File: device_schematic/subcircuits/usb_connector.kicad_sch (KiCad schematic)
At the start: 3 parts, among them J1 USB_B

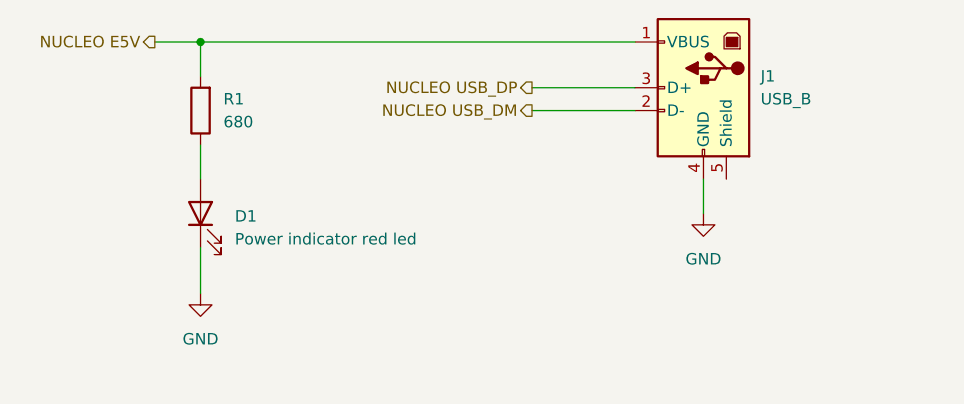
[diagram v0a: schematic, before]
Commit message: Device schematic finished version
+ correction to use D7 in place of D13
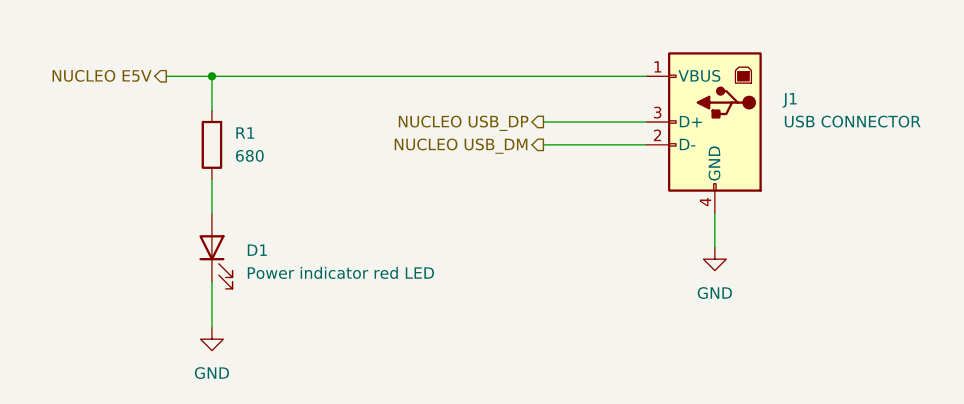
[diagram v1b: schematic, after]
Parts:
- D1: value Power indicator red led -> Power indicator red LED
- J1: value USB_B -> USB CONNECTOR
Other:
- moved on the sheet: D1, R1
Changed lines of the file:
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@@
 (kicad_sch (version 20211123) (generator eeschema)
   (paper "A4")
-  (junction (at 125.73 74.93) (diameter 0) (color 0 0 0 0)
+  (junction (at 127 78.74) (diameter 0) (color 0 0 0 0)
   )
-  (wire (pts (xy 162.56 82.55) (xy 173.99 82.55))
+  (wire (pts (xy 163.83 86.36) (xy 175.26 86.36))
     (stroke (width 0) (type default) (color 0 0 0 0))
   )
-  (wire (pts (xy 125.73 97.79) (xy 125.73 102.87))
+  (wire (pts (xy 127 101.6) (xy 127 106.68))
     (stroke (width 0) (type default) (color 0 0 0 0))
   )
-  (wire (pts (xy 125.73 74.93) (xy 125.73 78.74))
+  (wire (pts (xy 127 78.74) (xy 127 82.55))
     (stroke (width 0) (type default) (color 0 0 0 0))
   )
-  (wire (pts (xy 125.73 86.36) (xy 125.73 90.17))
+  (wire (pts (xy 127 90.17) (xy 127 93.98))
     (stroke (width 0) (type default) (color 0 0 0 0))
   )
-  (wire (pts (xy 181.61 90.17) (xy 181.61 93.98))
+  (wire (pts (xy 182.88 93.98) (xy 182.88 97.79))
     (stroke (width 0) (type default) (color 0 0 0 0))
   )
-  (wire (pts (xy 162.56 80.01) (xy 173.99 80.01))
+  (wire (pts (xy 163.83 83.82) (xy 175.26 83.82))
     (stroke (width 0) (type default) (color 0 0 0 0))
   )
-  (wire (pts (xy 125.73 74.93) (xy 173.99 74.93))
+  (wire (pts (xy 127 78.74) (xy 175.26 78.74))
     (stroke (width 0) (type default) (color 0 0 0 0))
   )
-  (wire (pts (xy 120.65 74.93) (xy 125.73 74.93))
+  (wire (pts (xy 121.92 78.74) (xy 127 78.74))
     (stroke (width 0) (type default) (color 0 0 0 0))
   )
-  (hierarchical_label "NUCLEO USB_DM" (shape output) (at 162.56 82.55 180)
+  (hierarchical_label "NUCLEO USB_DM" (shape output) (at 163.83 86.36 180)
     (effects (font (size 1.27 1.27)) (justify right))
   )
-  (hierarchical_label "NUCLEO USB_DP" (shape output) (at 162.56 80.01 180)
+  (hierarchical_label "NUCLEO USB_DP" (shape output) (at 163.83 83.82 180)
     (effects (font (size 1.27 1.27)) (justify right))
   )
-  (hierarchical_label "NUCLEO E5V" (shape output) (at 120.65 74.93 180)
+  (hierarchical_label "NUCLEO E5V" (shape output) (at 121.92 78.74 180)
     (effects (font (size 1.27 1.27)) (justify right))
   )
-  (symbol (lib_id "Device:R") (at 125.73 82.55 180) (unit 1)
+  (symbol (lib_id "Device:R") (at 127 86.36 180) (unit 1)
     (in_bom yes) (on_board yes) (fields_autoplaced)
-    (property "Reference" "R1" (id 0) (at 128.27 81.2799 0)
+    (property "Reference" "R1" (id 0) (at 129.54 85.0899 0)
       (effects (font (size 1.27 1.27)) (justify right))
     )
-    (property "Value" "680" (id 1) (at 128.27 83.8199 0)
+    (property "Value" "680" (id 1) (at 129.54 87.6299 0)
       (effects (font (size 1.27 1.27)) (justify right))
     )
-    (property "Footprint" "" (id 2) (at 127.508 82.55 90)
+    (property "Footprint" "" (id 2) (at 128.778 86.36 90)
       (effects (font (size 1.27 1.27)) hide)
     )
-    (property "Datasheet" "~" (id 3) (at 125.73 82.55 0)
+    (property "Datasheet" "~" (id 3) (at 127 86.36 0)
       (effects (font (size 1.27 1.27)) hide)
     )
@@
     (pin "2")
   )
-  (symbol (lib_id "Device:LED") (at 125.73 93.98 90) (unit 1)
+  (symbol (lib_id "Device:LED") (at 127 97.79 90) (unit 1)
     (in_bom yes) (on_board yes) (fields_autoplaced)
-    (property "Reference" "D1" (id 0) (at 129.54 94.2974 90)
+    (property "Reference" "D1" (id 0) (at 130.81 98.1074 90)
       (effects (font (size 1.27 1.27)) (justify right))
     )
-    (property "Value" "Power indicator red led" (id 1) (at 129.54 96.8374 90)
+    (property "Value" "Power indicator red LED" (id 1) (at 130.81 100.6474 90)
       (effects (font (size 1.27 1.27)) (justify right))
     )
-    (property "Footprint" "" (id 2) (at 125.73 93.98 0)
+    (property "Footprint" "" (id 2) (at 127 97.79 0)
       (effects (font (size 1.27 1.27)) hide)
     )
-    (property "Datasheet" "~" (id 3) (at 125.73 93.98 0)
+    (property "Datasheet" "~" (id 3) (at 127 97.79 0)
       (effects (font (size 1.27 1.27)) hide)
     )
@@
     (pin "2")
   )
-  (symbol (lib_id "Connector:USB_B") (at 181.61 80.01 0) (mirror y) (unit 1)
-    (in_bom yes) (on_board yes) (fields_autoplaced)
-    (property "Reference" "J1" (id 0) (at 187.96 78.7399 0)
+  (symbol (lib_id "Connector:USB_B") (at 182.88 83.82 0) (mirror y) (unit 1)
+    (in_bom yes) (on_board yes)
+    (property "Reference" "J1" (id 0) (at 190.5 81.28 0)
       (effects (font (size 1.27 1.27)) (justify right))
     )
-    (property "Value" "USB_B" (id 1) (at 187.96 81.2799 0)
+    (property "Value" "USB CONNECTOR" (id 1) (at 190.5 83.82 0)
       (effects (font (size 1.27 1.27)) (justify right))
     )
-    (property "Footprint" "" (id 2) (at 177.8 81.28 0)
+    (property "Footprint" "" (id 2) (at 186.69 85.09 0)
       (effects (font (size 1.27 1.27)) hide)
     )
-    (property "Datasheet" " ~" (id 3) (at 177.8 81.28 0)
+    (property "Datasheet" " ~" (id 3) (at 186.69 85.09 0)
       (effects (font (size 1.27 1.27)) hide)
     )
@@
     (pin "3")
     (pin "4")
-    (pin "5")
   )
-  (symbol (lib_id "power:GND") (at 181.61 93.98 0) (unit 1)
+  (symbol (lib_id "power:GND") (at 182.88 97.79 0) (unit 1)
     (in_bom yes) (on_board yes) (fields_autoplaced)
-    (property "Reference" "#PWR?" (id 0) (at 181.61 100.33 0)
+    (property "Reference" "#PWR?" (id 0) (at 182.88 104.14 0)
       (effects (font (size 1.27 1.27)) hide)
     )
-    (property "Value" "GND" (id 1) (at 181.61 99.06 0))
-    (property "Footprint" "" (id 2) (at 181.61 93.98 0)
+    (property "Value" "GND" (id 1) (at 182.88 102.87 0))
+    (property "Footprint" "" (id 2) (at 182.88 97.79 0)
       (effects (font (size 1.27 1.27)) hide)
     )
-    (property "Datasheet" "" (id 3) (at 181.61 93.98 0)
+    (property "Datasheet" "" (id 3) (at 182.88 97.79 0)
       (effects (font (size 1.27 1.27)) hide)
     )
     (pin "1")
   )
-  (symbol (lib_id "power:GND") (at 125.73 102.87 0) (unit 1)
+  (symbol (lib_id "power:GND") (at 127 106.68 0) (unit 1)
     (in_bom yes) (on_board yes) (fields_autoplaced)
-    (property "Reference" "#PWR?" (id 0) (at 125.73 109.22 0)
+    (property "Reference" "#PWR?" (id 0) (at 127 113.03 0)
       (effects (font (size 1.27 1.27)) hide)
     )
-    (property "Value" "GND" (id 1) (at 125.73 107.95 0))
-    (property "Footprint" "" (id 2) (at 125.73 102.87 0)
+    (property "Value" "GND" (id 1) (at 127 111.76 0))
+    (property "Footprint" "" (id 2) (at 127 106.68 0)
       (effects (font (size 1.27 1.27)) hide)
     )
-    (property "Datasheet" "" (id 3) (at 125.73 102.87 0)
+    (property "Datasheet" "" (id 3) (at 127 106.68 0)
       (effects (font (size 1.27 1.27)) hide)
     )
